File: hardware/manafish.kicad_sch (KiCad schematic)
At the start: 4 parts, among them J6 Battery, J8 USB_C_Receptacle_USB2.0_14P

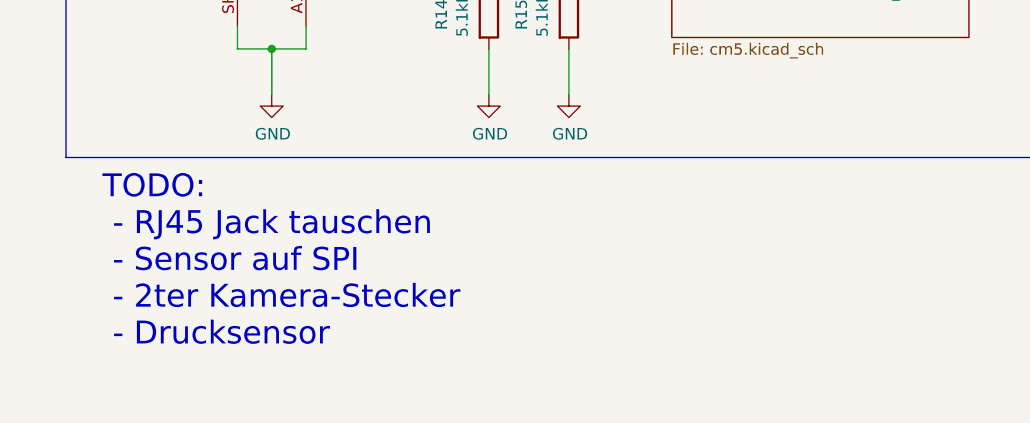
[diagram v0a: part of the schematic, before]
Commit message: Complete the power sheet and its part numbers
Schematic fixes from the power review:
- add the NTC bias network, PWR_FLAGs and the VOUTA capacitor C37
- rename VBAT to VSYS

Every power-sheet part now has Manufacturer, MPN, Mouser PN, Mouser and
Datasheet fields. All Mouser numbers were checked on 2026-10-09.

Part changes:
- the 10 uF/50 V caps (C26, C28, C30, C33, C34) are all TDK
  C3225X7R1H106K250AC in 1210; C26 and C30 move from 1206 to 1210
- C20 is a Nichicon UHW1V471MPD, same size as before; the Panasonic
  EEU-FR1V471 has a 37-week lead time, and the old Wurth number was 25 V
- C29 and C37 use Murata's in-production GCM parts; C25 and C27 use KEMET
- U6 and U7 are Lite-On LTV-817 (PC817 pinout)
- C21/C24 are valued 4.7nF 1kV to match the Wurth part, with a note on
  the 2 kV option

The SamacSys fields on D2-D5, Q1 and Q2 are renamed to the board's
standard field names.

Co-Authored-By: Claude Opus 5.5 <noreply@anthropic.com>
Claude-Session: https://claude.ai/code/session_01VySMh57b8sYaPe1qvNdeQG
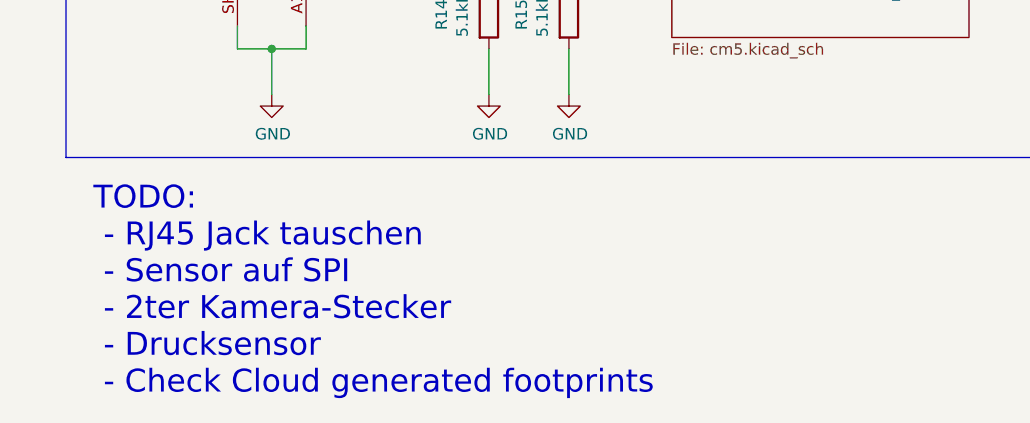
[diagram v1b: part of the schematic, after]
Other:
- note added: "TODO: - RJ45 Jack tauschen - Sensor auf SPI - 2ter Kamera-Stecker - Drucksensor - Check Cloud generated footprints"
- note removed: "TODO: - RJ45 Jack tauschen - Sensor auf SPI - 2ter Kamera-Stecker - Drucksensor"
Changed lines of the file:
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@@
 		)
 	)
-	(text "TODO:\n - RJ45 Jack tauschen\n - Sensor auf SPI\n - 2ter Kamera-Stecker\n - Drucksensor"
+	(text "TODO:\n - RJ45 Jack tauschen\n - Sensor auf SPI\n - 2ter Kamera-Stecker\n - Drucksensor\n - Check Cloud generated footprints"
 		(exclude_from_sim no)
-		(at 19.304 143.002 0)
+		(at 18.288 146.304 0)
 		(effects
 			(font

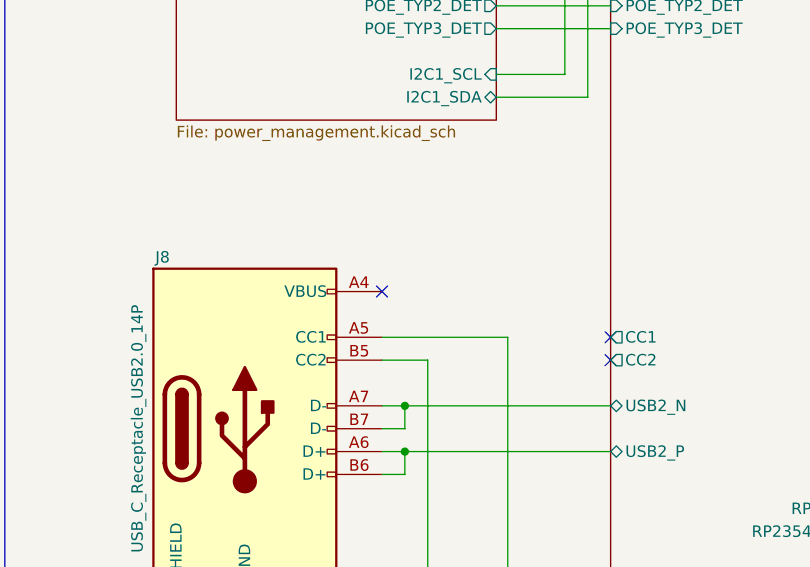
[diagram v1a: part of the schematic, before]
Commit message: Lay out the 4-layer PCB
Route the board on JLCPCB's JLC04161H-7628 stackup (4 layers, 1.6 mm,
ENIG). It fits a 74 mm tube centred on its axis; the tightest part is the
USB-C port J8, 1.8 mm from the wall. DRC gives 0 errors, 0 unconnected
items and a clean schematic parity check. 21 advisory warnings remain on
the 3 mm PoE isolation guide; the README lists them.

Layout:
- the PoE primary side keeps 2.0 mm from everything else on every layer,
  enforced by manafish.kicad_dru, with a primary-only island under U5's
  input half and inner-layer voids next to primary copper
- 100 ohm (Ethernet, CSI) and 90 ohm (USB) pair classes over a solid In1
  ground; GND pours on all layers with stitching vias
- RP2354A core regulator laid out per the RP2350 datasheet, including the
  In1 cut-out under VREG_LX
- fabrication, assembly and isolation-test notes on User.Comments

Schematic and BOM:
- U3 is now the YAGEO JXF0-1012NL 4-pair PoE MagJack, with a new YAGEO
  library and STEP model drawn from datasheet J520
- C21/C24 are 4.7 nF 2 kV KEMET C1812X472KGRACTU (1812)
- U6/U7 are LTV-817S-TA1 (SMD)
- J8's four VBUS pins are joined by a local VBUS label

Libraries:
- Silvertel Ag59800: keep-out on the module-facing layer and the inner
  layer next to it; pads 1-3, 8 and 9 solder-mask defined
- LTC4162 QFN: the exposed-pad paste windows clear the thermal vias
- ABM8-272-T3 courtyard trimmed; 3D model paths fixed for ABM8, SHT45 and
  BMI270

README: new PCB section (stackup, impedance, isolation, assembly,
testing) and the power and Ethernet descriptions brought up to date.
NOTICE: the YAGEO files and the library changes.

Co-Authored-By: Claude Opus 5.5 <noreply@anthropic.com>
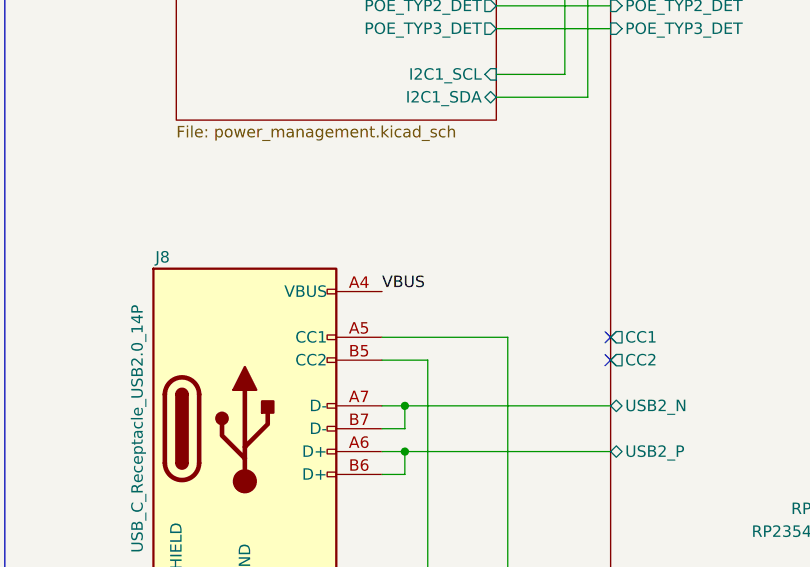
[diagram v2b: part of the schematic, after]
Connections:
- net VBUS: now reaches J8.A4 (VBUS), J8.A9 (VBUS), J8.B4 (VBUS), J8.B9 (VBUS)
- no-connect marks 4 -> 3
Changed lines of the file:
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@@
 		(at 82.55 83.82)
 	)
-	(no_connect
-		(at 57.15 78.74)
+	(label "VBUS"
+		(at 57.15 78.74 0)
+		(effects
+			(font
+				(size 1.27 1.27)
+			)
+			(justify left bottom)
+		)
 	)
 	(no_connect

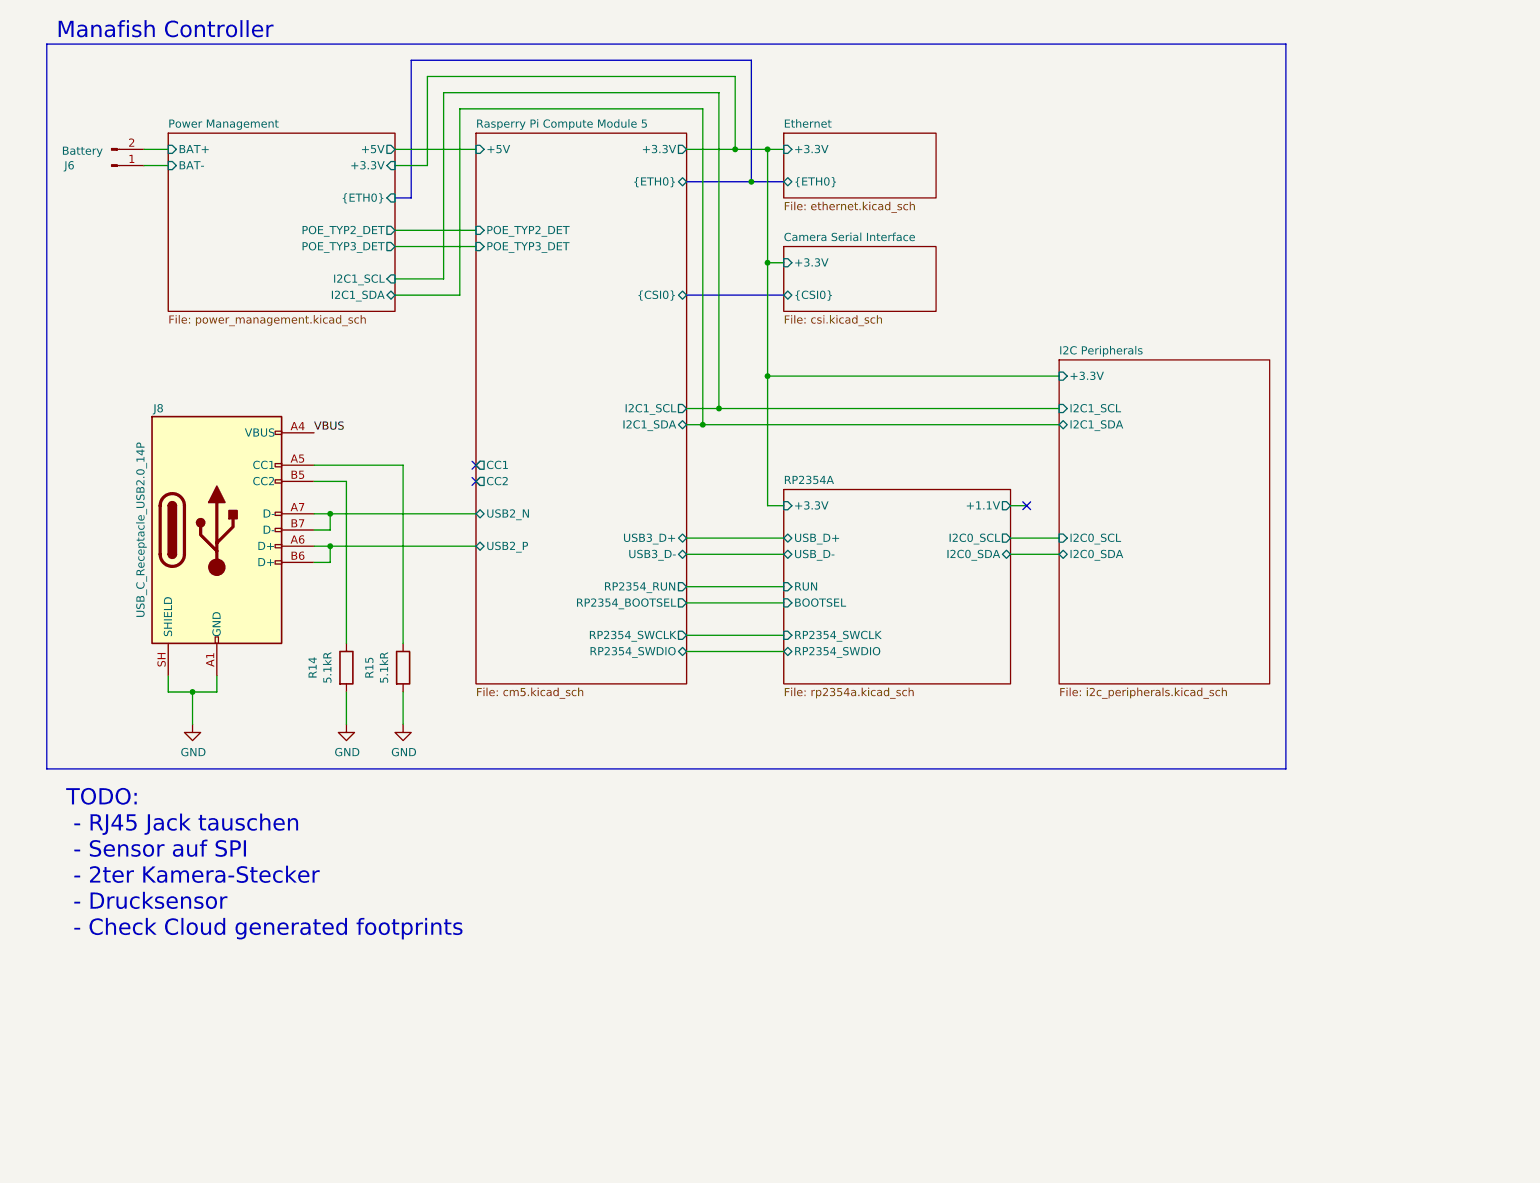
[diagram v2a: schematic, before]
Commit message: Add second camera, magnet load switch and schematic fixes
- Second camera J11 on MIPI1: I2C on ID_SD/ID_SC with 2.2k pull-ups,
  power enable on GPIO14/15 (CAM1_GPIO0/1); both cameras take 3.3 V
  from CM5_3.3V
- Magnet power switch: IC9 output is now +5V_AON, TPS22965 load switch
  IC15 drives +5V, J12 carries +5V_AON / MAG_ON / GND with R29
  pull-down; new TPS22965 symbol library
- Power: 4 A TPSM53604, 8 mOhm input sense resistor, C39/C40 bulk caps,
  F1-F3 battery polyfuses; 5 V raised to 5.115 V (R24 2.43k, 0.5 %
  feedback resistors); 47 uF at the CM5 5 V pins
- BMI270 on SPI and WSEN-PADS on I2C in serial_peripherals.kicad_sch
- Breakout headers J9/J13 with 5 V, 3.3 V and GND
- References renamed U -> IC; net classes for DPHY1, +5V, +5V_AON, +3.3V
- ERC clean (0 errors, 0 warnings); PCB update from the schematic is
  still in progress

Co-Authored-By: Claude Opus 5.5 <noreply@anthropic.com>
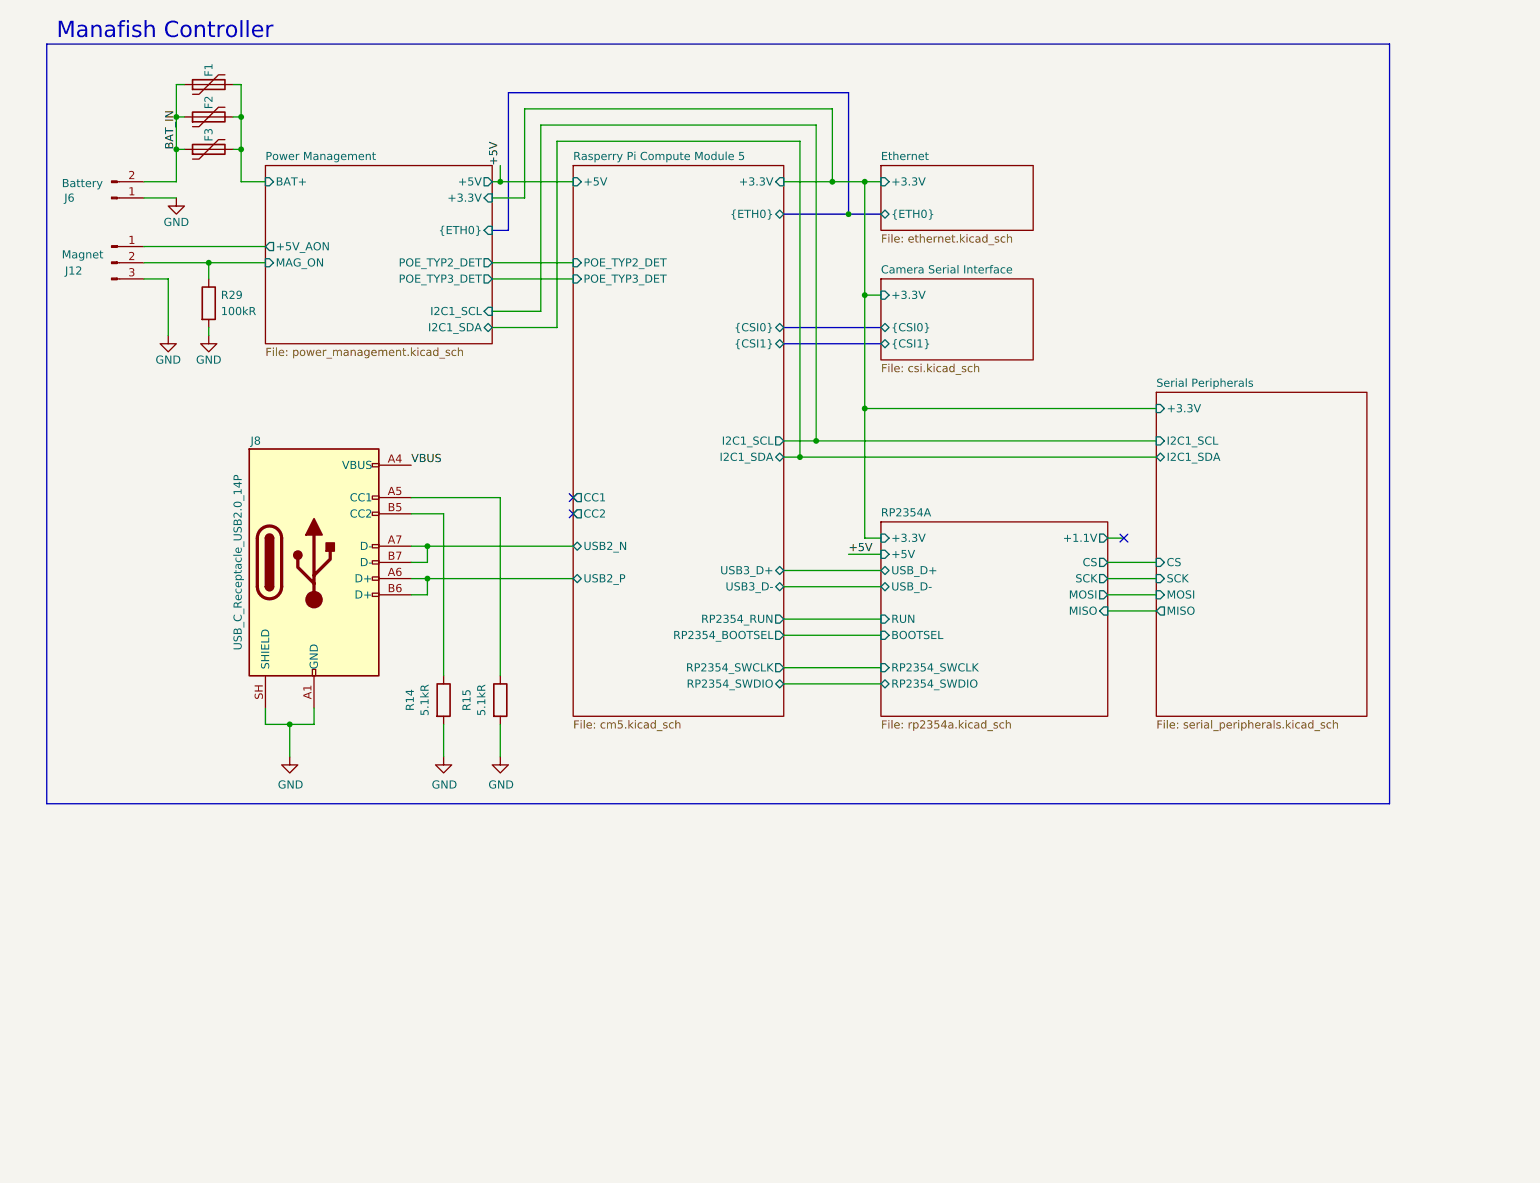
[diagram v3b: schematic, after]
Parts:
- added F1, F2, F3: MF-LSMF260/33X-2, Fuse:Fuse_2920_7451Metric, symbol Device:Polyfuse
- added J12: Magnet, Connector_JST:JST_GH_SM03B-GHS-TB_1x03-1MP_P1.25mm_Horizontal, symbol Connector:Conn_01x03_Pin
- added R29: 100kR, Resistor_SMD:R_0402_1005Metric, symbol Device:R
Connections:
- net Power Management/BAT- is gone; now on net GND: J6.1 (Pin_1)
- net GND: now also J12.3 (Pin_3), R29.2
- net Power Management/BAT+: now also F1.2, F2.2, F3.2; no longer J6.2 (Pin_2)
- new net BAT_IN: F1.1, F2.1, F3.1, J6.2 (Pin_2)
- new net Power Management/+5V_AON: J12.1 (Pin_1)
- new net Power Management/MAG_ON: J12.2 (Pin_2), R29.1
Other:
- sheet I2C Peripherals renamed Serial Peripherals
- sheet Camera Serial Interface ports: added {CSI1}; removed none
- sheet Power Management ports: added +5V_AON, MAG_ON; removed BAT-
- sheet RP2354A ports: added +5V, CS, MISO, MOSI, SCK; removed I2C0_SCL, I2C0_SDA
- sheet Rasperry Pi Compute Module 5 ports: added {CSI1}; removed none
- sheet Serial Peripherals: file i2c_peripherals.kicad_sch -> serial_peripherals.kicad_sch
- sheet Serial Peripherals ports: added CS, MISO, MOSI, SCK; removed I2C0_SCL, I2C0_SDA
- note removed: "TODO: - RJ45 Jack tauschen - Sensor auf SPI - 2ter Kamera-Stecker - Drucksensor - Check Cloud generated footprints"
- moved on the sheet: J6, J8, R14, R15
